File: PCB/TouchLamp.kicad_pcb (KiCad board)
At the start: 2 copper layers, 14 parts, among them IC1 ATTINY2313-P, P1 PWR_LED_ISP, P3 Sensor, Q1 BC817-40, U1 LM78L05

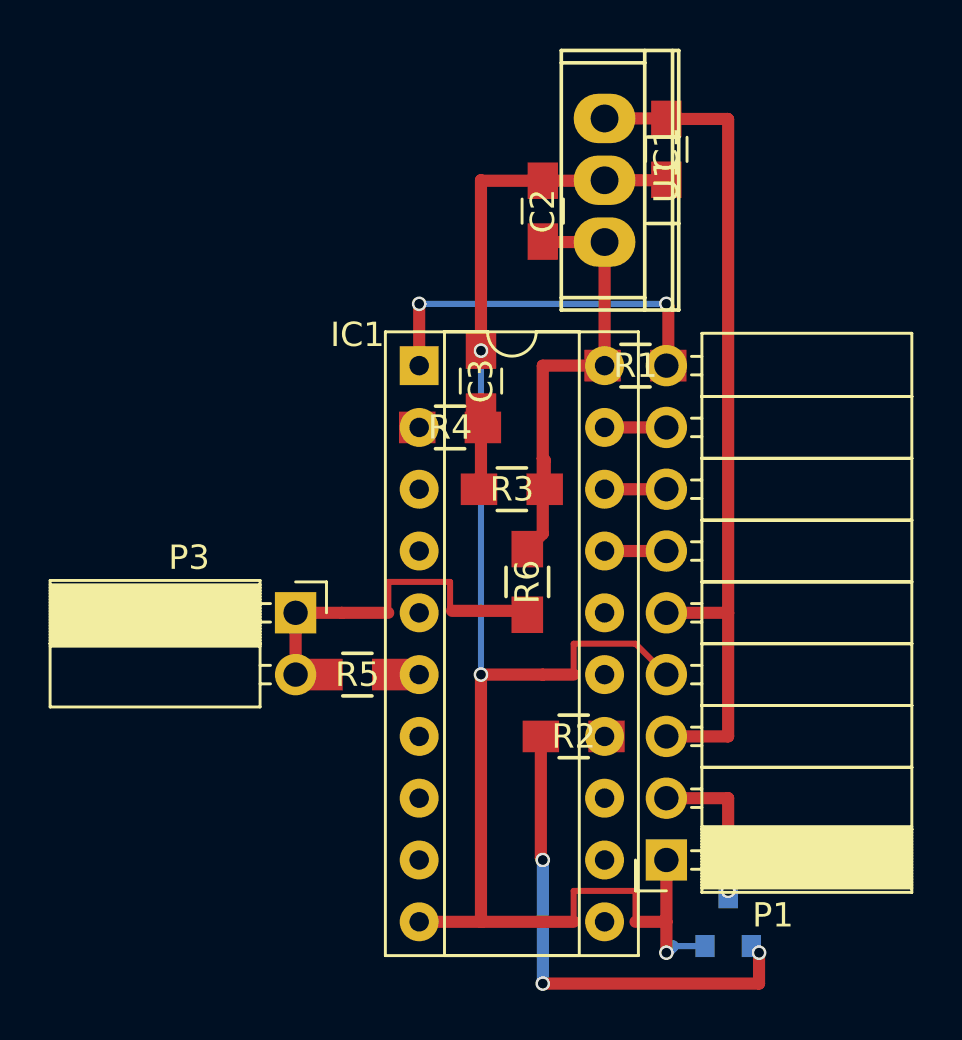
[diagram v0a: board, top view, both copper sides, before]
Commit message: optimized the PCB and adjusted the FW
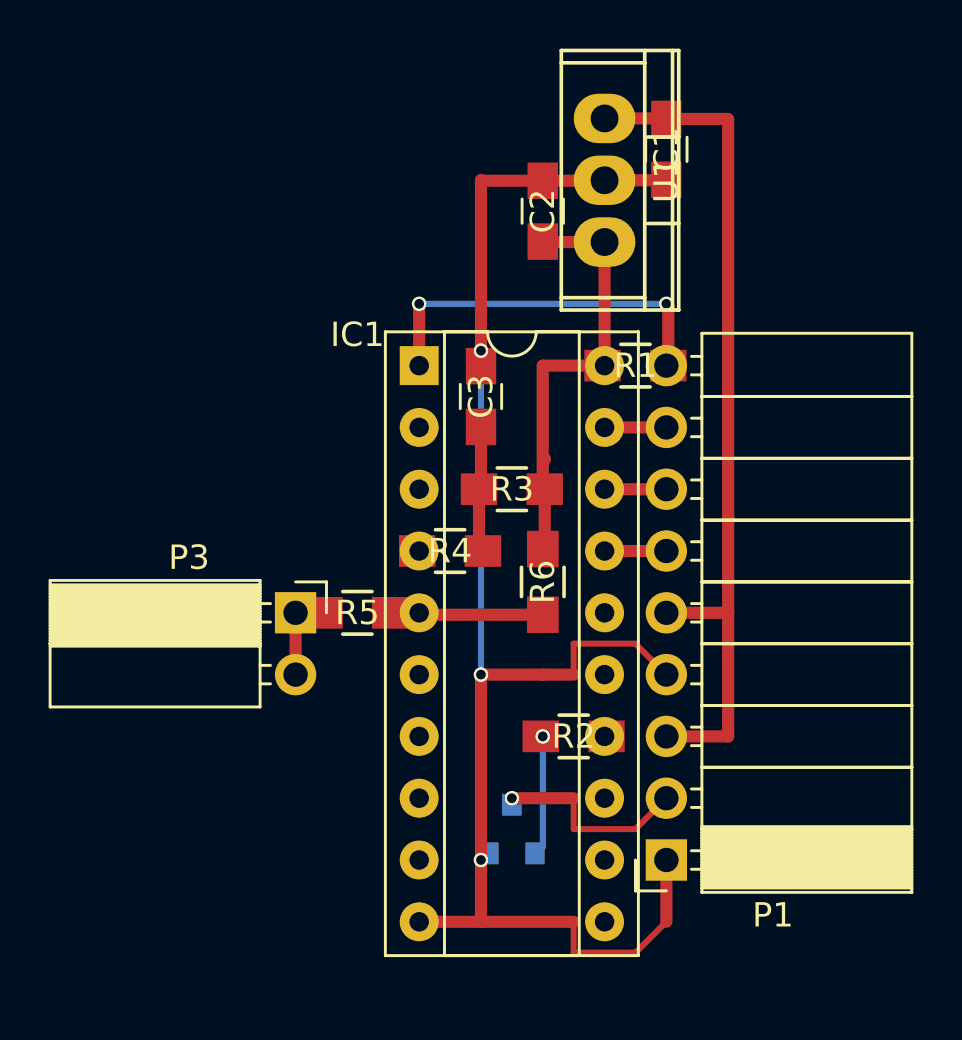
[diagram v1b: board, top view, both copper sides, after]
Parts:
- moved Q1 9.67 mm to (171.4, 95.2)
- moved R4 5.08 mm to (168.9, 83.8), turned to 180 degrees
- moved R5 2.54 mm to (165.1, 86.4), turned to 0 degrees
- moved C3 0.64 mm to (170.2, 77.5)
- moved R6 0.63 mm to (172.7, 85.1)
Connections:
- R4 pad 1: Net-(IC1-Pad2) -> Net-(C3-Pad2)
- R4 pad 2: Net-(C3-Pad2) -> Net-(IC1-Pad4)
- R5 pad 1: Net-(IC1-Pad6) -> Net-(P3-Pad1)
- R5 pad 2: Net-(P3-Pad1) -> Net-(IC1-Pad5)
- R6 pad 1: Net-(P3-Pad1) -> Net-(IC1-Pad5)
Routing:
- net Net-(Q1-Pad1): track 20.8 -> 5.05 mm, vias 3 -> 1
- net Net-(P3-Pad1): track 15.7 -> 3.73 mm
- net Net-(IC1-Pad5): track 0.00 -> 6.30 mm
- net GNDREF: track 65.8 -> 62.5 mm
- net Net-(C3-Pad2): track 3.12 -> 5.20 mm
- net Net-(P1-Pad2): track 6.62 -> 8.42 mm
- net Net-(C2-Pad1): track 19.5 -> 17.8 mm
- net Net-(IC1-Pad6): track 1.19 -> 0.00 mm
